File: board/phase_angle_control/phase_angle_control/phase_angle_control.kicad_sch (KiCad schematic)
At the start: 31 parts, among them J1 TB005-762-02BE, J2 TB005-762-02BE, J3 Conn_01x07, J4 Conn_02x04_Odd_Even, J5 Conn_02x04_Odd_Even, J6 Conn_02x04_Odd_Even, T1 Transformer_1P_1S, U1 STM32G030F6P, U2 PC3H4, U3 MOC3063S-TA1, U4 ACS71240

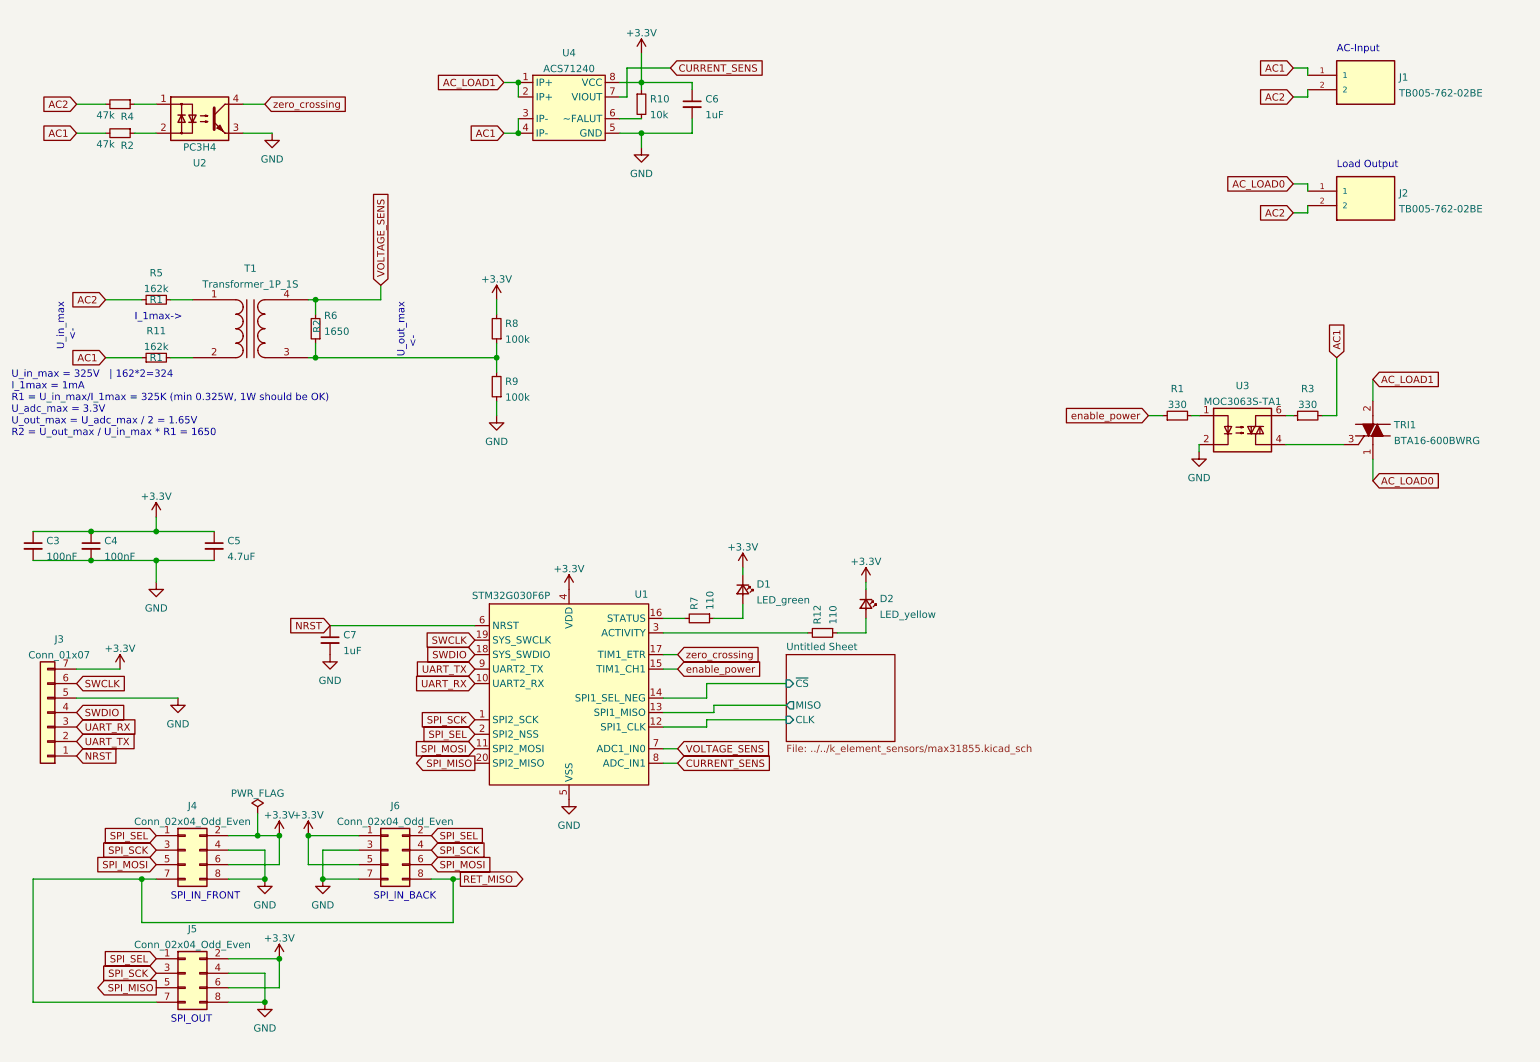
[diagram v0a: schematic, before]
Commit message: Redesign phase angle contrller board for more current throughput
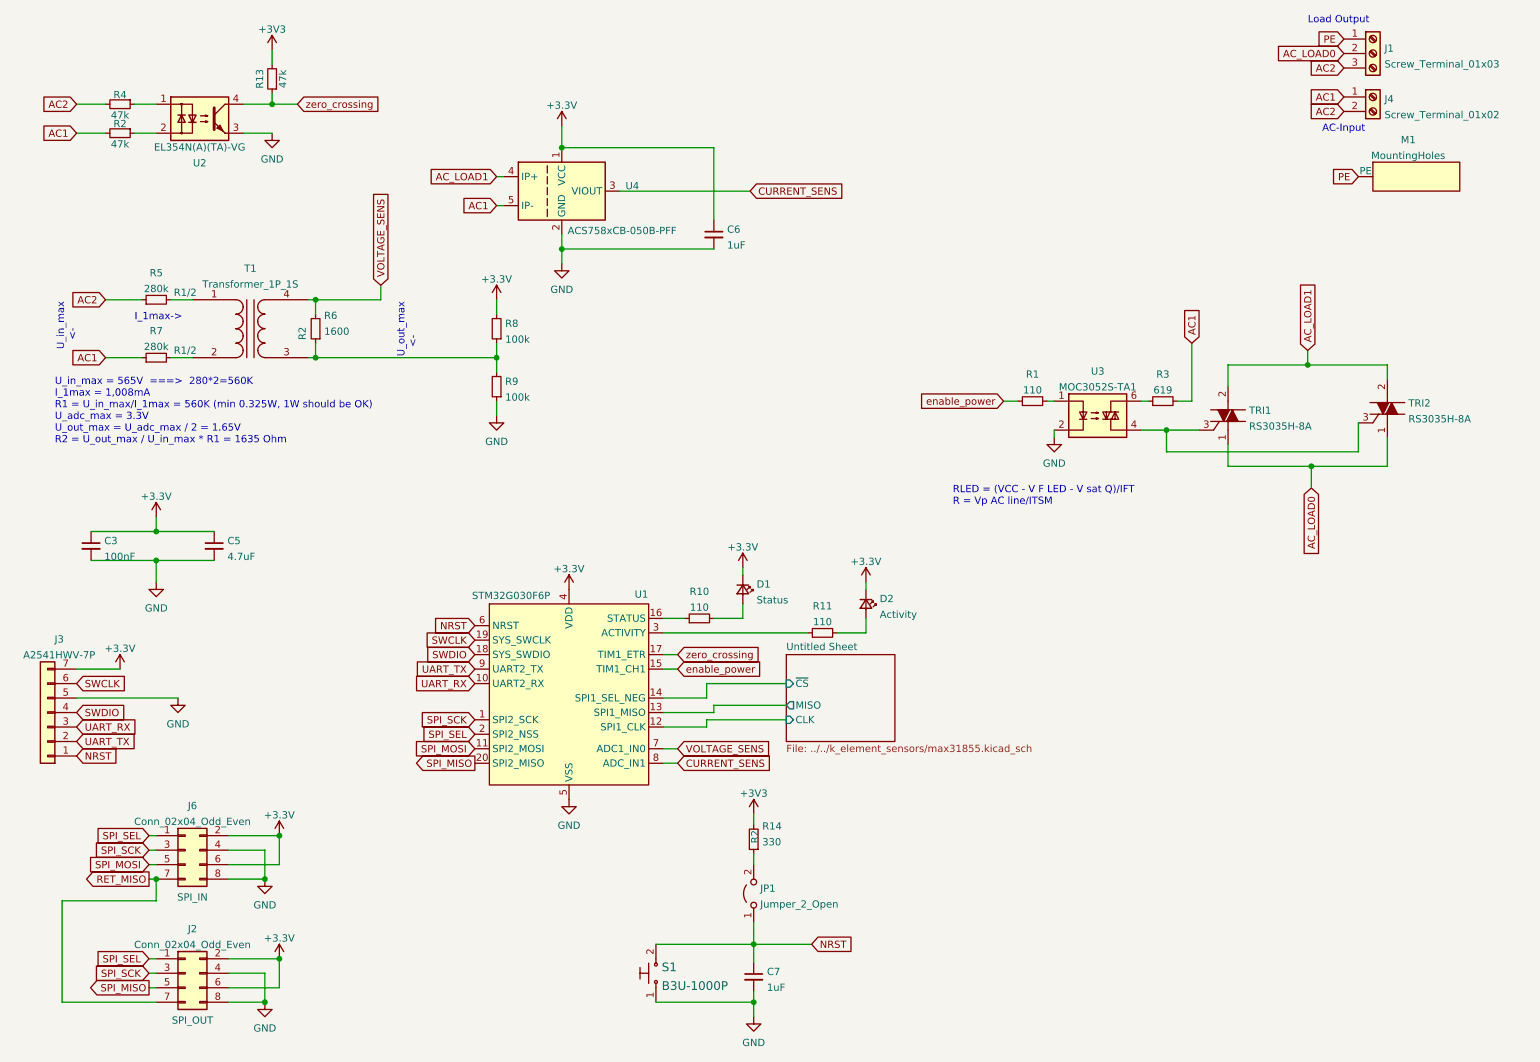
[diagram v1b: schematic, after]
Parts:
- removed C4: 100nF, Capacitor_SMD:C_0603_1608Metric_Pad1.08x0.95mm_HandSolder, symbol Device:C_Small
- removed J1, J2: TB005-762-02BE, pac:con_EB167A-02-H, symbol TB005-762-02BE:TB005-762-02BE
- removed J4, J5: Conn_02x04_Odd_Even, Connector_PinHeader_2.54mm:PinHeader_2x04_P2.54mm_Vertical_SMD, symbol Connector_Generic:Conn_02x04_Odd_Even
- removed R12: 110, Resistor_SMD:R_0603_1608Metric_Pad0.98x0.95mm_HandSolder, symbol Device:R_Small
- removed U4: ACS71240, Package_SO:SOIC-8_3.9x4.9mm_P1.27mm, symbol phase_angle_control:ACS71240
- added J1: Screw_Terminal_01x03, pac:KF206B-7.5-3P, symbol Connector:Screw_Terminal_01x03
- added J2: Conn_02x04_Odd_Even, Connector_PinHeader_2.54mm:PinHeader_2x04_P2.54mm_Horizontal, symbol Connector_Generic:Conn_02x04_Odd_Even
- added J4: Screw_Terminal_01x02, pac:KF206B-7.5-2P, symbol Connector:Screw_Terminal_01x02
- added JP1: Jumper_2_Open, Jumper:SolderJumper-2_P1.3mm_Open_RoundedPad1.0x1.5mm, symbol Jumper:Jumper_2_Open
- added M1: MountingHoles, pac:MountingHolesPE, symbol phase_angle_control:MountingHoles
- added R13: 47k, Resistor_SMD:R_0603_1608Metric_Pad0.98x0.95mm_HandSolder, symbol Device:R_Small
- added R14: 330, Resistor_SMD:R_0603_1608Metric_Pad0.98x0.95mm_HandSolder, symbol Device:R_Small
- added S1: B3U-1000P, Button_Switch_SMD:SW_Push_SPST_NO_Alps_SKRK, symbol dk_Tactile-Switches:B3U-1000P
- added TRI2: RS3035H-8A, Package_TO_SOT_THT:TO-220-3_Vertical, symbol dk_Thyristors-TRIACs:BTA16-600BWRG
- added U4: ACS758xCB-050B-PFF, Sensor_Current:Allegro_CB_PFF, symbol Sensor_Current:ACS758xCB-050B-PFF
- C3: LCSC Part# (none) -> C191538
- C5: LCSC Part# (none) -> C651001
- C6, C7: LCSC Part# (none) -> C393692
- D1: value LED_green -> Status; footprint LED_SMD:LED_0201_0603Metric_Pad0.64x0.40mm_HandSolder -> LED_SMD:LED_0603_1608Metric_Pad1.05x0.95mm_HandSolder; LCSC Part# (none) -> C273616
- D2: value LED_yellow -> Activity; footprint LED_SMD:LED_0201_0603Metric_Pad0.64x0.40mm_HandSolder -> LED_SMD:LED_0603_1608Metric_Pad1.05x0.95mm_HandSolder; LCSC Part# (none) -> C192667
- J3: value Conn_01x07 -> A2541HWV-7P; footprint Connector_PinHeader_2.54mm:PinHeader_1x07_P2.54mm_Vertical -> Connector_PinSocket_2.54mm:PinSocket_1x07_P2.54mm_Vertical; LCSC Part# (none) -> C225504
- J6: footprint Connector_PinHeader_2.54mm:PinHeader_2x04_P2.54mm_Vertical_SMD -> Connector_PinHeader_2.54mm:PinHeader_2x04_P2.54mm_Horizontal; Comment (none) -> SPI_IN; LCSC Part# (none) -> C358706
- R1: value 330 -> 110; footprint Resistor_SMD:R_1206_3216Metric_Pad1.30x1.75mm_HandSolder -> Resistor_SMD:R_0603_1608Metric_Pad0.98x0.95mm_HandSolder; LCSC Part# (none) -> C203247
- R10: value 10k -> 110; LCSC Part# (none) -> C203247
- R11: value 162k -> 110; footprint Resistor_SMD:R_2010_5025Metric_Pad1.40x2.65mm_HandSolder -> Resistor_SMD:R_0603_1608Metric_Pad0.98x0.95mm_HandSolder; LCSC Part# (none) -> C203247; RefName R1 -> (none)
- R2, R4: LCSC Part# (none) -> C104822
- R3: value 330 -> 619; LCSC Part# (none) -> C247212
- R5: value 162k -> 280k; footprint Resistor_SMD:R_2010_5025Metric_Pad1.40x2.65mm_HandSolder -> Resistor_SMD:R_1210_3225Metric_Pad1.30x2.65mm_HandSolder; LCSC Part# (none) -> C422336; RefName R1 -> R1/2
- R6: value 1650 -> 1600; LCSC Part# (none) -> C186398
- R7: value 110 -> 280k; footprint Resistor_SMD:R_0603_1608Metric_Pad0.98x0.95mm_HandSolder -> Resistor_SMD:R_1210_3225Metric_Pad1.30x2.65mm_HandSolder; LCSC Part# (none) -> C422336; RefName (none) -> R1/2
- R8, R9: LCSC Part# (none) -> C203223
- T1: LCSC Part# (none) -> C125191; LCSL Part# (none) -> C125191
- TRI1: value BTA16-600BWRG -> RS3035H-8A; Category Discrete Semiconductor Products -> (none); DK_Datasheet_Link http://www.st.com/content/ccc/resource/technical/document/d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 -> (none); DK_Detail_Page /product-detail/en/stmicroelectronics/BTA16-600BWRG/497-312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 -> (none); Digi-Key_PN 497-3122-5-ND -> (none); Family Thyristors - TRIACs -> (none); LCSC Part# (none) -> C246522; MPN BTA16-600BWRG -> (none)
- U1: LCSC Part# (none) -> C724040
- U2: value PC3H4 -> EL354N(A)(TA)-VG; LCSC Part# (none) -> C146213
- U3: value MOC3063S-TA1 -> MOC3052S-TA1; LCSC Part# (none) -> C115471
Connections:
- net +3V3: now also J6.2 (Pin_2), J6.6 (Pin_6), J2.2 (Pin_2), J2.6 (Pin_6), R13.2, R14.2, U4.1 (VCC); no longer J6.1 (Pin_1), J6.5 (Pin_5), R10.1
- net AC1: now also R7.1, J4.1 (Pin_1), U4.5 (IP-); no longer R11.1
- net AC2: now also J1.3 (Pin_3), J4.2 (Pin_2)
- net AC_LOAD0: now also J1.2 (Pin_2), TRI2.1 (A1)
- net AC_LOAD1: now also TRI2.2 (A2), U4.4 (IP+)
- net CURRENT_SENS: now also U4.3 (VIOUT)
- net GND: now also J6.4 (Pin_4), J6.8 (Pin_8), J2.4 (Pin_4), J2.8 (Pin_8), S1.1, U4.2 (GND); no longer J6.3 (Pin_3), J6.7 (Pin_7)
- net NRST: now also JP1.1 (A), S1.2
- net RET_MISO: now also J6.7 (Pin_7), J2.7 (Pin_7); no longer J6.8 (Pin_8)
- net SPI_MISO: now also J2.5 (Pin_5)
- net SPI_MOSI: now also J6.5 (Pin_5); no longer J6.6 (Pin_6)
- net SPI_SCK: now also J6.3 (Pin_3), J2.3 (Pin_3); no longer J6.4 (Pin_4)
- net SPI_SEL: now also J6.1 (Pin_1), J2.1 (Pin_1); no longer J6.2 (Pin_2)
- net zero_crossing: now also R13.1
- net at T1.2 (AB): now also R7.2; no longer R11.2
- net at R10.2: now also D1.2 (A)
- net at U1.16 (STATUS): now also R10.1; no longer R7.2
- net at U1.3 (ACTIVITY): now also R11.1
- net at D2.2 (A): now also R11.2
- net at TRI1.3 (G), U3.4: now also TRI2.3 (G)
- new net: JP1.2 (B), R14.1
- new net PE: J1.1 (Pin_1), M1.1 (PE)
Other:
- note added: "RLED = (VCC - V F LED - V sat Q)/IFT R = Vp AC line/ITSM"
- note added: "U_in_max = 565V ===> 280*2=560K I_1max = 1,008mA R1 = U_in_max/I_1max = 560K (min 0.325W, 1W should be OK) U_adc_max = 3.3V U_out_max = U_adc_max / 2 = 1.65V R2 = U_out_max / U_in_max * R1 = 1635 Ohm"
- note removed: "SPI_IN_BACK"
- note removed: "SPI_IN_FRONT"
- note removed: "SPI_OUT"
- note removed: "U_in_max = 325V | 162*2=324 I_1max = 1mA R1 = U_in_max/I_1max = 325K (min 0.325W, 1W should be OK) U_adc_max = 3.3V U_out_max = U_adc_max / 2 = 1.65V R2 = U_out_max / U_in_max * R1 = 1650"
- moved on the sheet: C3, C6, J6, R1, R3, TRI1, U3

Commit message: Update phase-angle-control-board to handle more current
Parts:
- R4: LCSC Part# C104822 -> (none); Supplier and ref (none) -> C104822
- S1: footprint Button_Switch_SMD:SW_Push_SPST_NO_Alps_SKRK -> digikey-footprints:Switch_Tactile_SMD_B3U-1000P
- TRI1, TRI2: footprint Package_TO_SOT_THT:TO-220-3_Vertical -> digikey-footprints:TO-220-3; Category (none) -> Discrete Semiconductor Products; DK_Datasheet_Link (none) -> http://www.st.com/content/ccc/resource/technical/document/d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; DK_Detail_Page (none) -> /product-detail/en/stmicroelectronics/BTA16-600BWRG/497-312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; Digi-Key_PN (none) -> 497-3122-5-ND; Family (none) -> Thyristors - TRIACs; MPN (none) -> BTA16-600BWRG
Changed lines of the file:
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@@
       (effects (font (size 1.27 1.27)) hide)
     )
-    (property "LCSC Part#" "C104822" (id 4) (at 38.1 29.21 90)
+    (property "Supplier and ref" "C104822" (id 4) (at 38.1 29.21 90)
       (effects (font (size 1.27 1.27)) hide)
     )
@@
       (effects (font (size 1.524 1.524)) (justify right))
     )
-    (property "Footprint" "Button_Switch_SMD:SW_Push_SPST_NO_Alps_SKRK" (id 2) (at 127 176.53 0)
+    (property "Footprint" "digikey-footprints:Switch_Tactile_SMD_B3U-1000P" (id 2) (at 127 176.53 0)
       (effects (font (size 1.524 1.524)) (justify left) hide)
     )
@@
       (effects (font (size 1.27 1.27)) (justify left))
     )
-    (property "Footprint" "Package_TO_SOT_THT:TO-220-3_Vertical" (id 2) (at 237.49 78.74 0)
+    (property "Footprint" "digikey-footprints:TO-220-3" (id 2) (at 237.49 78.74 0)
       (effects (font (size 1.27 1.27)) (justify left) hide)
     )
-    (property "Datasheet" "https://datasheet.lcsc.com/lcsc/1810182025_Shenzhen-Haoruijia-Elec--RS3035H-8A_C246522.pdf" (id 3) (at 237.49 76.2 0)
+    (property "Datasheet" "http://www.st.com/content/ccc/resource/technical/document/datasheet/67/06/bc/c9/35/8e/4f/ea/CD00002265.pdf/files/CD00002265.pdf/jcr:content/translations/en.CD00002265.pdf" (id 3) (at 237.49 76.2 0)
       (effects (font (size 1.524 1.524)) (justify left) hide)
     )
@@
       (effects (font (size 1.524 1.524)) (justify left) hide)
     )
+    (property "Digi-Key_PN" "497-3122-5-ND" (id 8) (at 237.49 73.66 0)
+      (effects (font (size 1.524 1.524)) (justify left) hide)
+    )
+    (property "MPN" "BTA16-600BWRG" (id 9) (at 237.49 71.12 0)
+      (effects (font (size 1.524 1.524)) (justify left) hide)
+    )
+    (property "Category" "Discrete Semiconductor Products" (id 10) (at 237.49 68.58 0)
+      (effects (font (size 1.524 1.524)) (justify left) hide)
+    )
+    (property "Family" "Thyristors - TRIACs" (id 11) (at 237.49 66.04 0)
+      (effects (font (size 1.524 1.524)) (justify left) hide)
+    )
+    (property "DK_Datasheet_Link" "http://www.st.com/content/ccc/resource/technical/document/datasheet/67/06/bc/c9/35/8e/4f/ea/CD00002265.pdf/files/CD00002265.pdf/jcr:content/translations/en.CD00002265.pdf" (id 12) (at 237.49 63.5 0)
+      (effects (font (size 1.524 1.524)) (justify left) hide)
+    )
+    (property "DK_Detail_Page" "/product-detail/en/stmicroelectronics/BTA16-600BWRG/497-3122-5-ND/654430" (id 13) (at 237.49 60.96 0)
+      (effects (font (size 1.524 1.524)) (justify left) hide)
+    )
     (pin "1")
     (pin "2")
@@
       (effects (font (size 1.27 1.27)) (justify left))
     )
-    (property "Footprint" "Package_TO_SOT_THT:TO-220-3_Vertical" (id 2) (at 265.43 77.47 0)
+    (property "Footprint" "digikey-footprints:TO-220-3" (id 2) (at 265.43 77.47 0)
       (effects (font (size 1.27 1.27)) (justify left) hide)
     )
-    (property "Datasheet" "https://datasheet.lcsc.com/lcsc/1810182025_Shenzhen-Haoruijia-Elec--RS3035H-8A_C246522.pdf" (id 3) (at 265.43 74.93 0)
+    (property "Datasheet" "http://www.st.com/content/ccc/resource/technical/document/datasheet/67/06/bc/c9/35/8e/4f/ea/CD00002265.pdf/files/CD00002265.pdf/jcr:content/translations/en.CD00002265.pdf" (id 3) (at 265.43 74.93 0)
       (effects (font (size 1.524 1.524)) (justify left) hide)
     )
@@
     )
     (property "Status" "Active" (id 12) (at 265.43 52.07 0)
+      (effects (font (size 1.524 1.524)) (justify left) hide)
+    )
+    (property "Digi-Key_PN" "497-3122-5-ND" (id 8) (at 265.43 72.39 0)
+      (effects (font (size 1.524 1.524)) (justify left) hide)
+    )
+    (property "MPN" "BTA16-600BWRG" (id 9) (at 265.43 69.85 0)
+      (effects (font (size 1.524 1.524)) (justify left) hide)
+    )
+    (property "Category" "Discrete Semiconductor Products" (id 10) (at 265.43 67.31 0)
+      (effects (font (size 1.524 1.524)) (justify left) hide)
+    )
+    (property "Family" "Thyristors - TRIACs" (id 11) (at 265.43 64.77 0)
+      (effects (font (size 1.524 1.524)) (justify left) hide)
+    )
+    (property "DK_Datasheet_Link" "http://www.st.com/content/ccc/resource/technical/document/datasheet/67/06/bc/c9/35/8e/4f/ea/CD00002265.pdf/files/CD00002265.pdf/jcr:content/translations/en.CD00002265.pdf" (id 12) (at 265.43 62.23 0)
+      (effects (font (size 1.524 1.524)) (justify left) hide)
+    )
+    (property "DK_Detail_Page" "/product-detail/en/stmicroelectronics/BTA16-600BWRG/497-3122-5-ND/654430" (id 13) (at 265.43 59.69 0)
       (effects (font (size 1.524 1.524)) (justify left) hide)
     )
@@
     (pin "5")
   )
-  (symbol (lib_name "STM32G030F6P_1") (lib_id "MCU_ST_STM32G0:STM32G030F6P") (at 116.84 132.08 0) (unit 1)
+  (symbol (lib_id "MCU_ST_STM32G0:STM32G030F6P") (at 116.84 132.08 0) (unit 1)
     (in_bom yes) (on_board yes)
     (property "Reference" "U1" (id 0) (at 129.54 115.1594 0))
@@
     )
     (path "/311b9d9f-5d45-4c7c-ada0-338ff5c43123"
-      (reference "S1") (unit 1) (value "B3U-1000P") (footprint "Button_Switch_SMD:SW_Push_SPST_NO_Alps_SKRK")
+      (reference "S1") (unit 1) (value "B3U-1000P") (footprint "digikey-footprints:Switch_Tactile_SMD_B3U-1000P")
     )
     (path "/15f9e367-b73e-4e28-9ba4-eb2ca6e0f255"
@@
     )
     (path "/6143df9e-e49e-46b3-9bbd-0cff368c856c"
-      (reference "TRI1") (unit 1) (value "RS3035H-8A") (footprint "Package_TO_SOT_THT:TO-220-3_Vertical")
+      (reference "TRI1") (unit 1) (value "RS3035H-8A") (footprint "digikey-footprints:TO-220-3")
     )
     (path "/fa12b1e5-f14b-4284-aa83-e78baf067082"
-      (reference "TRI2") (unit 1) (value "RS3035H-8A") (footprint "Package_TO_SOT_THT:TO-220-3_Vertical")
+      (reference "TRI2") (unit 1) (value "RS3035H-8A") (footprint "digikey-footprints:TO-220-3")
     )
     (path "/3283c6b8-d722-4fa8-88ca-786cd8fc7b9d"
